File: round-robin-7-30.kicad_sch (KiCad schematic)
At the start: 72 parts

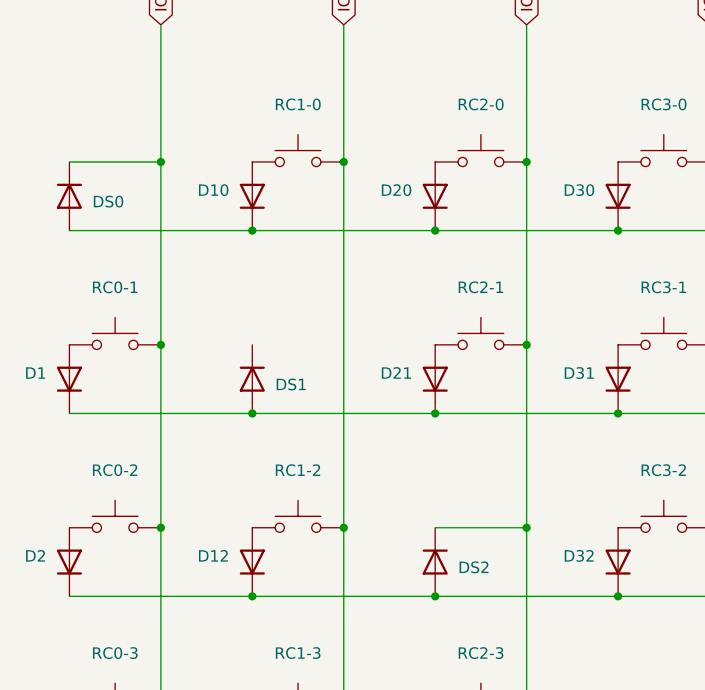
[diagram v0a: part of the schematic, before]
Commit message: Add missing connector on DS1
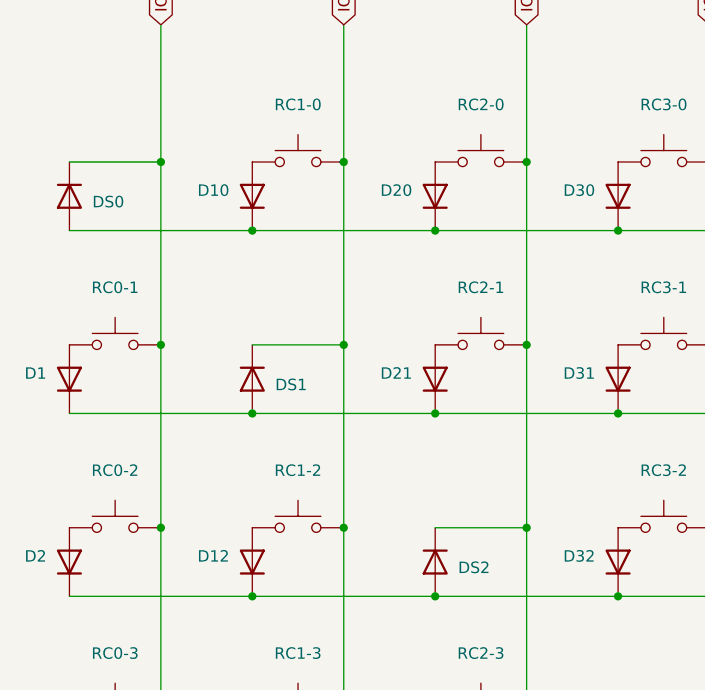
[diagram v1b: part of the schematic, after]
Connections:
- net IO 1: now also DS1.1 (K)
